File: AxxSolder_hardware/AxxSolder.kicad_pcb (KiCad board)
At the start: 2 copper layers, 39 x 82.5 mm, 147 parts, among them IC1 TLV76733DRVR, IC2 OPA2387DSGT, IC3 LMR54406DBVR, IC4 STM32G431CBT6, IC5 TPD4E1U06DBVR, IC6 STUSB4500QTR, IC7 MAX16171ATA_VY+T, IC8 LTC4440AHMS8E, IC9 INA281A5QDBVRQ1, J1 USB4110-GF-A, J2 691243110009, J3 TSW-102-07-T-S, J4 61300611821, J5 TSW-102-07-T-S, J6 TSW-102-07-T-S, J7 TSW-108-07-T-S, Q1 STL9P3LLH6, Q2 STL10N3LLH5, Q3 2N7002NXAKR, U2 PEC11J-9215F-S0015, U3 BSC014N04LS

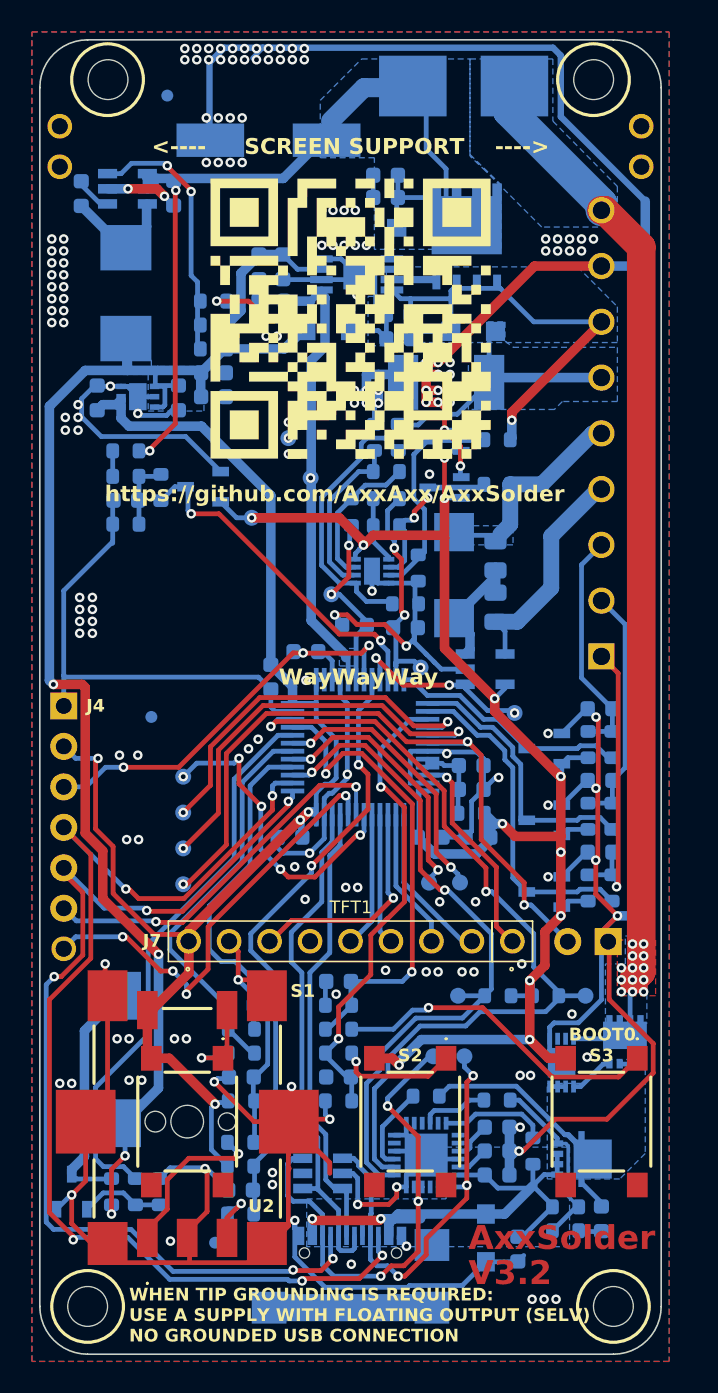
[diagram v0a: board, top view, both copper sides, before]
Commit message: feat: Change logos and silscreen texts
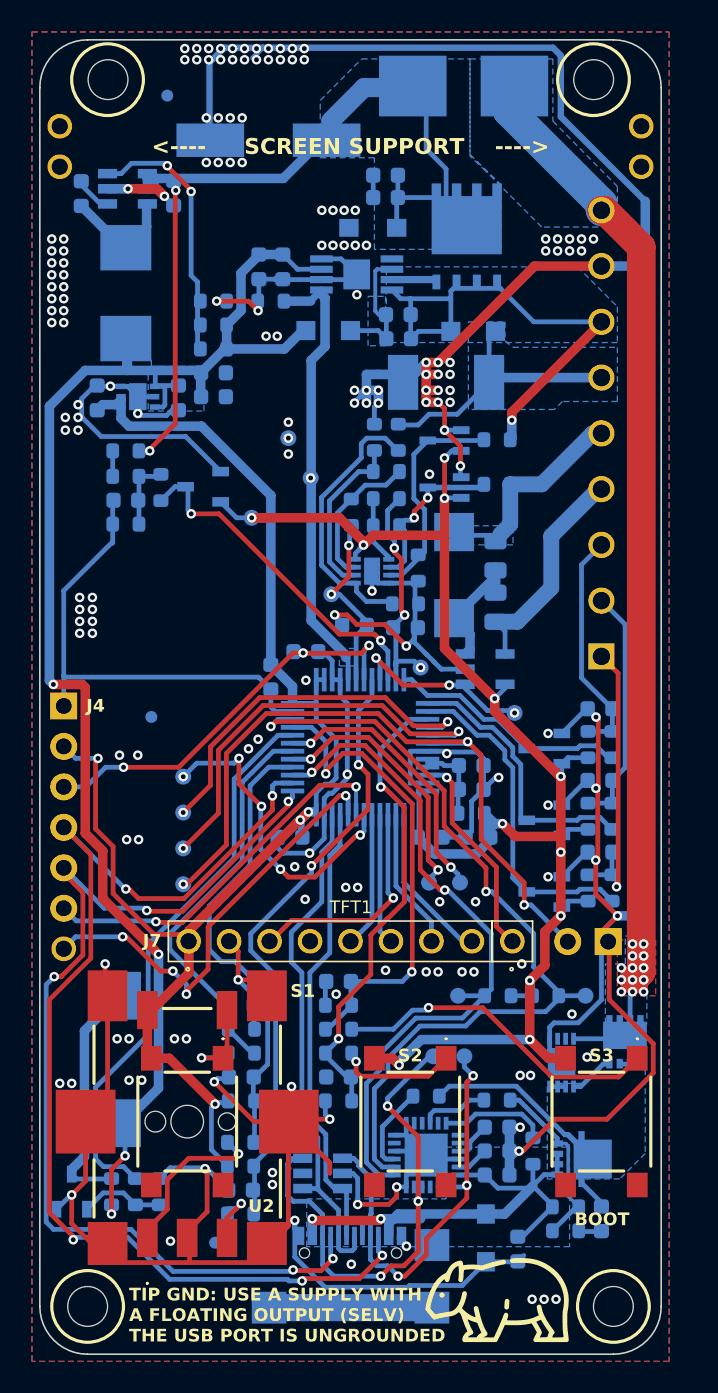
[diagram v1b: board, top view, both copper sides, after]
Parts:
- removed G***: LOGO, LOGO
- added wombat_logo_back***: wombat_logo_back, wombat_logo:wombat_logo_back, F.Cu at (169.6, 101.5)
- added wombat_logo_front***: wombat_logo_front, wombat_logo:wombat_logo_front, F.Cu at (189.7, 146.6)
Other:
- board text added: "Axel Johansson"
- board text added: "BOOT"
- board text added: "By: AxxAxx"
- board text added: "TIP GND: USE A SUPPLY WITH A FLOATING OUTPUT (SELV) THE USB PORT IS UNGROUNDED"
- board text removed: "2025-03"
- board text removed: "AxxAxx"
- board text removed: "AxxSolder"
- board text removed: "BOOT0"
- board text removed: "NEVER SOLDER ON LIVE CIRCUITS!"
- board text removed: "V3.2"
- board text removed: "WHEN TIP GROUNDING IS REQUIRED: USE A SUPPLY WITH FLOATING OUTPUT (SELV) NO GROUNDED USB CONNECTION"
- board text removed: "WayWayWay"
- board text removed: "https://github.com/AxxAxx/AxxSolder"
